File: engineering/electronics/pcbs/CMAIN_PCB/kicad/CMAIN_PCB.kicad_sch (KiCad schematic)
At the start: 73 parts, among them IC1 TSYS01, J1 RPI_5_WITH_SSQ-120-01-F-D, J10 1778719, J11 M9N-G4-3100, J12 1778719, J13 1778719, J14 XT30PW-F, J15 SM04B-GHS-TB_LF__SN_, J16 1778719, J17 SM03B-GHS-TB(LF)(SN), J18 SM04B-GHS-TB_LF__SN_, J19 1778719, J2 1778719, J20 SM04B-GHS-TB_LF__SN_, J21 1778719, J22 SM04B-GHS-TB_LF__SN_, J23 1814948, J24 1778719, J27 1814948, J29 1778735, J3 AXK6S00547YG, J30 1778735, J31 1814951, J32 1814948, J33 USB4216-03-A, J35 SM04B-GHS-TB_LF__SN_, J36 SM05B-GHS-TB_LF__SN_, J37 1778719, J38 1778719, J39 1814935, J4 AXK6S00547YG, J40 1814948, J41 SM06B-GHS-TB_LF__SN_, J43 1814948, J46 1814951, J49 1814935, J5 SM04B-GHS-TB_LF__SN_, J50 1814935, J53 1814935, J54 SM04B-GHS-TB_LF__SN_, J6 1778719, J7 SM04B-GHS-TB_LF__SN_, J8 1814935, J9 SM04B-GHS-TB_LF__SN_, U10 SMTSO25100CTJ, U11 SMTSO25100CTJ, U12 SMTSO25100CTJ, U3 SMTSOM380BTR, U5 C7429635, U6 SMTSOM380BTR, U7 SMTSOM380BTR, U8 SMTSOM380BTR, U9 SMTSO25100CTJ

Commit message: Import linked CMAIN PCB layout
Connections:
- net CAN2_H: now also R14.1, S2.1 (NC_1)
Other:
- sheet can_circuit renamed CAN_circuit
- sheet ethernet renamed Ethernet
- sheet power_control renamed Power_control
- sheet power_supply renamed Power_supply
- note added: "Temporary power-source flags for new power_supply architecture; replace with explicit hierarchical power pins once final regulator/distribution nets are locked."
- moved on the sheet: C1, IC1, J1, J10, J13, J15, J16, J18, J2, J20, J21, J22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

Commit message: electronics: update CMAIN and CBC PCB files
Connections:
- net CAN2_H: no longer R14.1, S2.1 (NC_1)
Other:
- moved on the sheet: J23, J27, J32, J40

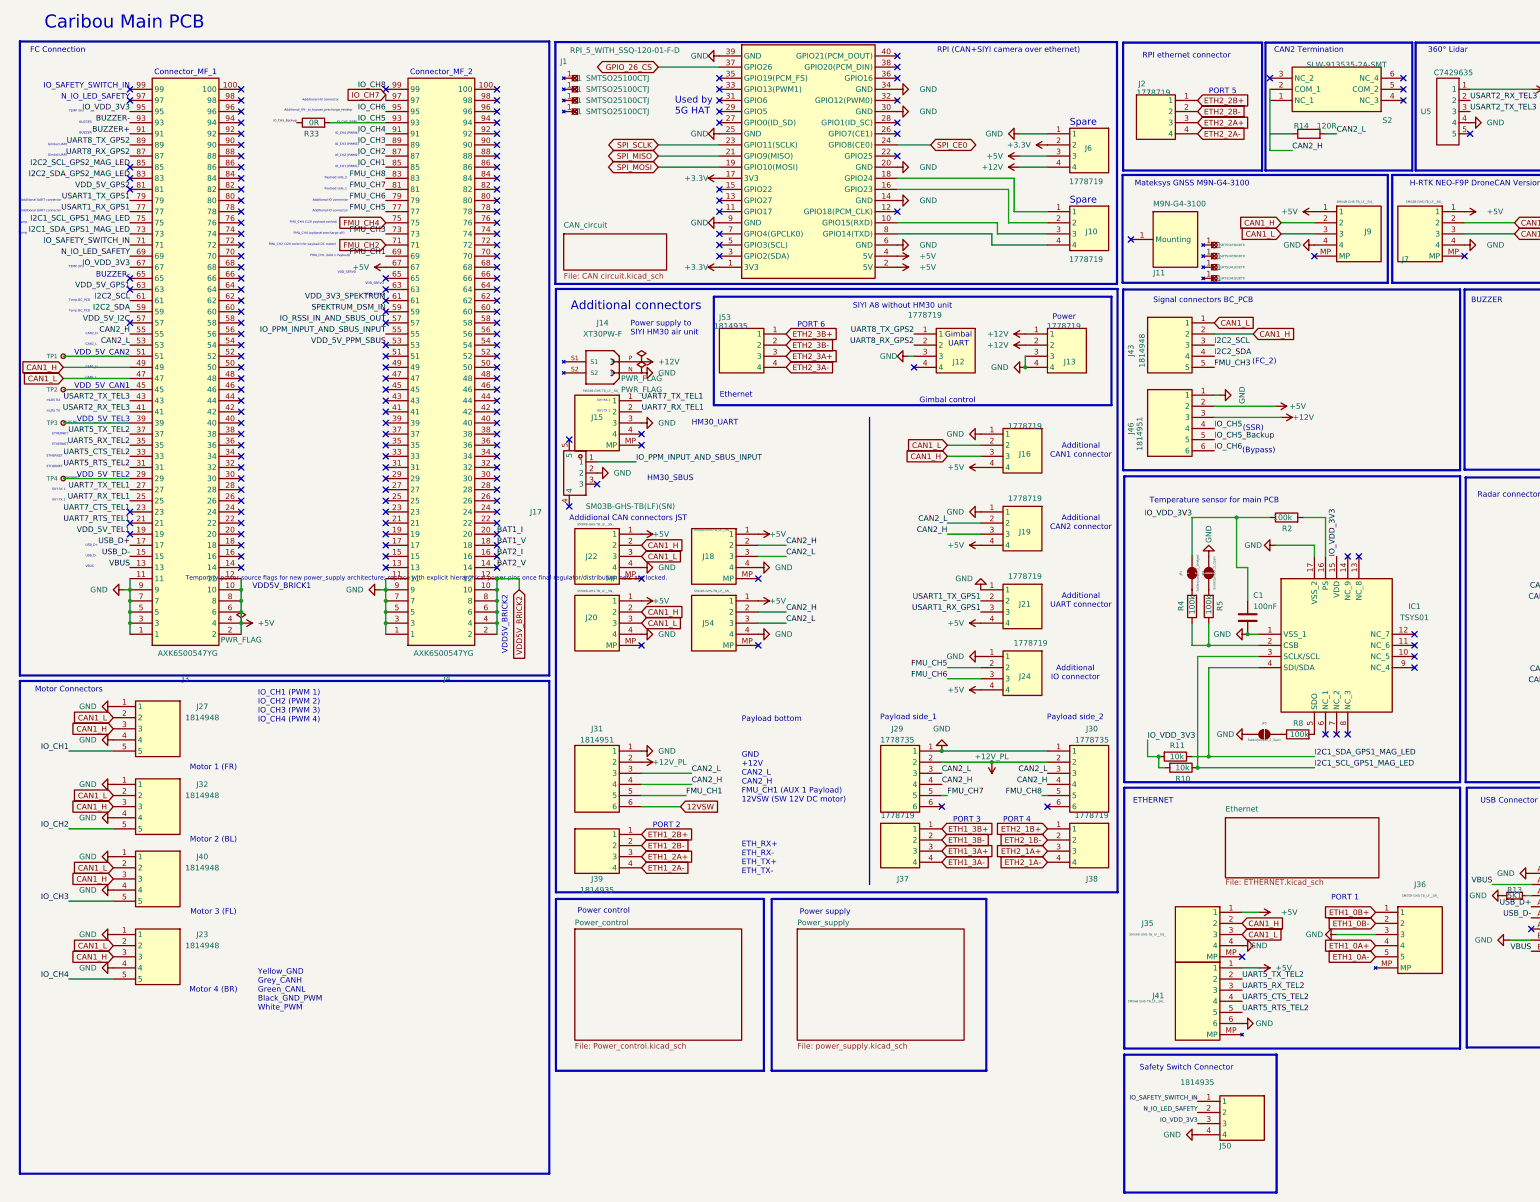
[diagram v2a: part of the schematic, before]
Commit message: electronics: integrate June PCB updates
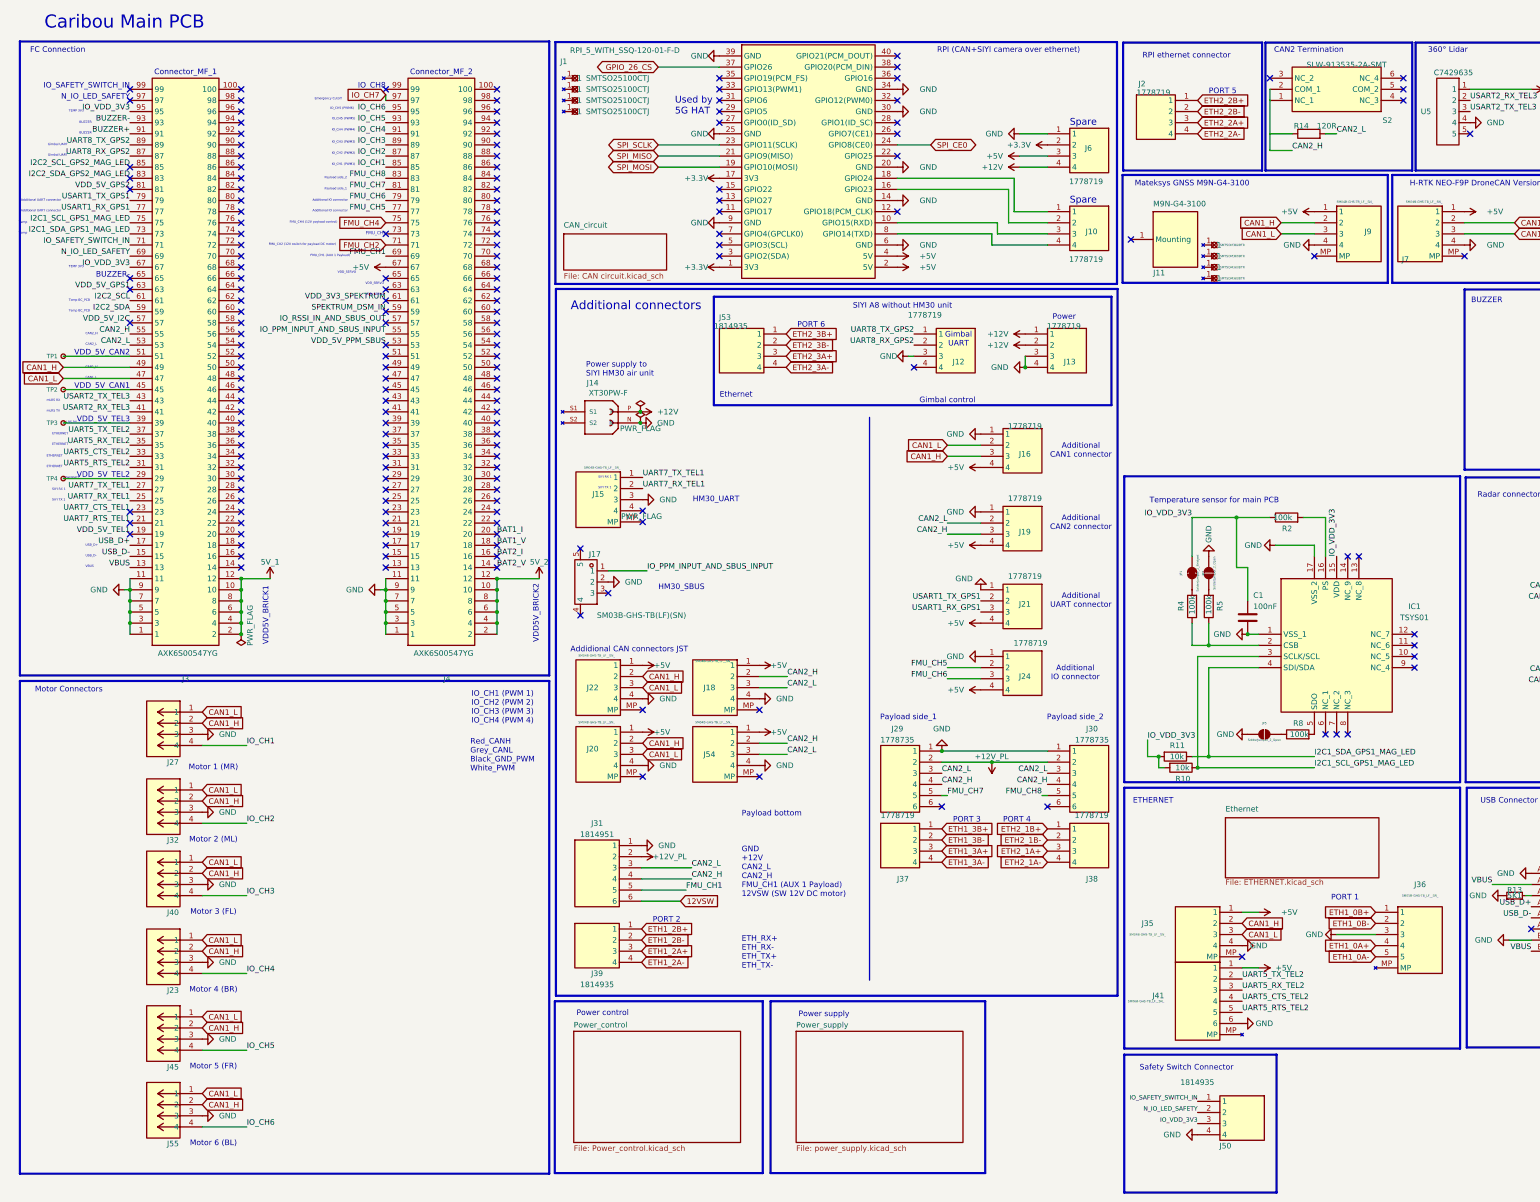
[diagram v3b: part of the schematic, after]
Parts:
- removed J43: 1814948, Samacsys:1814948, symbol Samacsys_kicad_sym:1814948
- removed J46: 1814951, Samacsys:1814951, symbol Samacsys_kicad_sym:1814951
- removed R33: 0R, Resistor_SMD:R_0805_2012Metric_Pad1.20x1.40mm_HandSolder, symbol Device:R
- added J45, J55: ${ALTIUM_VALUE}, CMAIN_PCB:AT13-4P, symbol CMAIN_PCB:AT13-4P
- J23, J27, J32, J40: value 1814948 -> ${ALTIUM_VALUE}; footprint Samacsys:1814948 -> CMAIN_PCB:AT13-4P; symbol Samacsys_kicad_sym:1814948 -> CMAIN_PCB:AT13-4P; Height 5.1 -> (none); MFR (none) -> Amphenol SINE Systems; MPN (none) -> AT13-4P; Manufacturer_Name Phoenix Contact -> (none); Manufacturer_Part_Number 1814948 -> (none); Mouser Part Number 651-1814948 -> (none); Mouser Price/Stock https://www.mouser.co.uk/ProductDetail/Phoenix-Contact/1814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 -> (none)
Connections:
- net +5V: no longer J3.10, J3.12, J3.2, J3.4, J3.6, J3.8
- net CAN1_H: now also J23.2, J27.2, J32.2, J40.2, J45.2, J55.2; no longer J23.3, J27.3, J32.3, J40.3
- net CAN1_L: now also J23.1, J27.1, J32.1, J40.1, J45.1, J55.1; no longer J23.2, J27.2, J32.2, J40.2
- net GND: now also J23.3, J27.3, J32.3, J40.3, J45.3, J55.3; no longer J23.1, J23.4, J27.1, J27.4, J32.1, J32.4, J40.1, J40.4
- net IO_CH1: now also J27.4; no longer J27.5
- net IO_CH2: now also J32.4; no longer J32.5
- net IO_CH3: now also J40.4; no longer J40.5
- net IO_CH4: now also J23.4; no longer J23.5
- net IO_CH5: now also J45.4
- net IO_CH6: now also J55.4
- net FMU_CH3: no longer names the net of J4.73
- net IO_CH8: no longer names the net of J4.99
- net VDD5V_BRICK2 renamed 5V_2
- new net 5V_1: J3.10, J3.12, J3.2, J3.4, J3.6, J3.8
- no-connect marks 182 -> 183
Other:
- note added: "Emergency Cutoff"
- note added: "FMU_CH3"
- note added: "IO_CH5 (PWM5)"
- note added: "IO_CH8"
- note added: "Motor 1 (MR)"
- note added: "Motor 2 (ML)"
- note added: "Motor 5 (FR)"
- note added: "Motor 6 (BL)"
- note added: "Red_CANH Grey_CANL Black_GND_PWM White_PWM"
- note removed: "(Bypass)"
- note removed: "(FC_2)"
- note removed: "(SSR)"
- note removed: "Additional HV connector"
- note removed: "FMU_CH4 (optional precharge off)"
- note removed: "IO_CH5 (SSR)"
- note removed: "Motor 1 (FR)"
- note removed: "Motor 2 (BL)"
- note removed: "Signal connectors BC_PCB"
- note removed: "Temporary power-source flags for new power_supply architecture; replace with explicit hierarchical power pins once final regulator/distribution nets are locked."
- note removed: "Yellow_GND Grey_CANH Green_CANL Black_GND_PWM White_PWM"
- moved on the sheet: J14, J15, J17, J18, J20, J22, J31, J39, J54

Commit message: electronics: clean up CMAIN local libraries
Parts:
- C1: footprint Capacitor_SMD:C_0805_2012Metric_Pad1.18x1.45mm_HandSolder -> CMAIN_PCB:C_0805_2012Metric_Pad1.18x1.45mm_HandSolder
- J14: footprint Snapeda:XT30PW-F_AMASS_XT30PW-F -> CMAIN_PCB:XT30PW-F_AMASS_XT30PW-F
- J15, J18, J20, J22, J35, J5, J54, J7: footprint Samacsys:SM04B-GHS-TB -> CMAIN_PCB:SM04B-GHS-TB
- J17: footprint EasyEDA_Lib:CONN-TH_SM03B-GHS-TB-LF-SN -> CMAIN_PCB:CONN-TH_SM03B-GHS-TB-LF-SN
- J23, J27, J32, J40: footprint CMAIN_PCB:AT13-4P -> CMAIN_PCB:1814948
- J29, J30: footprint Samacsys:1778735 -> CMAIN_PCB:1778735
- J3, J4: footprint Samacsys:AXK6S00547YG -> CMAIN_PCB:AXK6S00547YG
- J31: footprint Samacsys:1814951 -> CMAIN_PCB:1814951
- J33: footprint Samacsys:USB421603A -> CMAIN_PCB:USB421603A
- J36: footprint Samacsys:SM05B-GHS-TB -> CMAIN_PCB:SM05B-GHS-TB
- J39, J49, J50, J53, J8: footprint Samacsys:1814935 -> CMAIN_PCB:1814935
- J41: footprint Samacsys:SM06B-GHS-TB -> CMAIN_PCB:SM06B-GHS-TB
- J9: footprint Samacsys:SM04B-GHS-TB -> CMAIN_PCB:SM04B-GHS-TB_J9
- JP1: footprint Snapeda:SolderJumper-2_P1.3mm_Bridged2Bar_RoundedPad1.0x1.5mm -> CMAIN_PCB:SolderJumper-2_P1.3mm_Bridged2Bar_RoundedPad1.0x1.5mm
- JP2, JP5: footprint Snapeda:SolderJumper-2_P1.3mm_Open_RoundedPad1.0x1.5mm -> CMAIN_PCB:SolderJumper-2_P1.3mm_Open_RoundedPad1.0x1.5mm
- LS1: footprint Samacsys:CMT8530SSMTTR -> CMAIN_PCB:CMT8530SSMTTR
- R10, R11, R12, R13, R14, R2, R4, R5, R8: footprint Resistor_SMD:R_0805_2012Metric_Pad1.20x1.40mm_HandSolder -> CMAIN_PCB:R_0805_2012Metric_Pad1.20x1.40mm_HandSolder
- U5: footprint EasyEDA_Lib:CONN-TH_5P-P2.50_ZX-XH2.54-5PZZ -> CMAIN_PCB:CONN-TH_5P-P2.50_ZX-XH2.54-5PZZ
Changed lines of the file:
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@@
 			)
 		)
-		(property "Footprint" "Samacsys:SM04B-GHS-TB"
+		(property "Footprint" "CMAIN_PCB:SM04B-GHS-TB"
 			(at 275.59 314.96 0)
 			(hide yes)
@@
 			)
 		)
-		(property "Footprint" "Samacsys:1778735"
+		(property "Footprint" "CMAIN_PCB:1778735"
 			(at 264.16 278.13 0)
 			(hide yes)
@@
 			)
 		)
-		(property "Footprint" "Snapeda:SolderJumper-2_P1.3mm_Bridged2Bar_RoundedPad1.0x1.5mm"
+		(property "Footprint" "CMAIN_PCB:SolderJumper-2_P1.3mm_Bridged2Bar_RoundedPad1.0x1.5mm"
 			(at 280.67 142.24 0)
 			(hide yes)
@@
 			)
 		)
-		(property "Footprint" "Samacsys:AXK6S00547YG"
+		(property "Footprint" "CMAIN_PCB:AXK6S00547YG"
 			(at 118.11 62.23 0)
 			(hide yes)
@@
 			)
 		)
-		(property "Footprint" "Samacsys:SM04B-GHS-TB"
+		(property "Footprint" "CMAIN_PCB:SM04B-GHS-TB"
 			(at 326.39 154.94 0)
 			(hide yes)
@@
 			)
 		)
-		(property "Footprint" "Capacitor_SMD:C_0805_2012Metric_Pad1.18x1.45mm_HandSolder"
+		(property "Footprint" "CMAIN_PCB:C_0805_2012Metric_Pad1.18x1.45mm_HandSolder"
 			(at 294.64 156.21 0)
 			(hide yes)
@@
 			)
 		)
-		(property "Footprint" "Snapeda:SolderJumper-2_P1.3mm_Open_RoundedPad1.0x1.5mm"
+		(property "Footprint" "CMAIN_PCB:SolderJumper-2_P1.3mm_Open_RoundedPad1.0x1.5mm"
 			(at 297.18 179.07 0)
 			(hide yes)
@@
 			)
 		)
-		(property "Footprint" "Resistor_SMD:R_0805_2012Metric_Pad1.20x1.40mm_HandSolder"
+		(property "Footprint" "CMAIN_PCB:R_0805_2012Metric_Pad1.20x1.40mm_HandSolder"
 			(at 307.34 43.18 90)
 			(hide yes)
@@
 			)
 		)
-		(property "Footprint" "Samacsys:SM06B-GHS-TB"
+		(property "Footprint" "CMAIN_PCB:SM06B-GHS-TB"
 			(at 275.59 327.66 0)
 			(hide yes)
@@
 			)
 		)
-		(property "Footprint" "CMAIN_PCB:AT13-4P"
+		(property "Footprint" "CMAIN_PCB:1814948"
 			(at 39.116 213.868 0)
 			(hide yes)
@@
 			)
 		)
-		(property "Footprint" "Samacsys:SM04B-GHS-TB"
+		(property "Footprint" "CMAIN_PCB:SM04B-GHS-TB"
 			(at 138.684 214.376 0)
 			(hide yes)
@@
 			)
 		)
-		(property "Footprint" "Samacsys:SM04B-GHS-TB"
+		(property "Footprint" "CMAIN_PCB:SM04B-GHS-TB"
 			(at 165.354 258.572 0)
 			(hide yes)
@@
 			)
 		)
-		(property "Footprint" "Samacsys:SM04B-GHS-TB"
+		(property "Footprint" "CMAIN_PCB:SM04B-GHS-TB"
 			(at 363.22 154.94 0)
 			(hide yes)
@@
 			)
 		)
-		(property "Footprint" "Resistor_SMD:R_0805_2012Metric_Pad1.20x1.40mm_HandSolder"
+		(property "Footprint" "CMAIN_PCB:R_0805_2012Metric_Pad1.20x1.40mm_HandSolder"
 			(at 276.86 182.88 90)
 			(hide yes)
@@
 			)
 		)
-		(property "Footprint" "Snapeda:XT30PW-F_AMASS_XT30PW-F"
+		(property "Footprint" "CMAIN_PCB:XT30PW-F_AMASS_XT30PW-F"
 			(at 149.606 105.41 0)
 			(hide yes)
@@
 			)
 		)
-		(property "Footprint" "Samacsys:1814935"
+		(property "Footprint" "CMAIN_PCB:1814935"
 			(at 375.92 257.81 0)
 			(hide yes)
@@
 			)
 		)
-		(property "Footprint" "EasyEDA_Lib:CONN-TH_SM03B-GHS-TB-LF-SN"
+		(property "Footprint" "CMAIN_PCB:CONN-TH_SM03B-GHS-TB-LF-SN"
 			(at 143.51 144.272 0)
 			(hide yes)
@@
 			)
 		)
-		(property "Footprint" "Samacsys:SM05B-GHS-TB"
+		(property "Footprint" "CMAIN_PCB:SM05B-GHS-TB"
 			(at 339.09 314.96 0)
 			(hide yes)
@@
 			)
 		)
-		(property "Footprint" "Samacsys:SM04B-GHS-TB"
+		(property "Footprint" "CMAIN_PCB:SM04B-GHS-TB"
 			(at 138.684 272.542 0)
 			(hide yes)
@@
 			)
 		)
-		(property "Footprint" "Resistor_SMD:R_0805_2012Metric_Pad1.20x1.40mm_HandSolder"
+		(property "Footprint" "CMAIN_PCB:R_0805_2012Metric_Pad1.20x1.40mm_HandSolder"
 			(at 304.8 180.34 90)
 			(hide yes)
@@
 			)
 		)
-		(property "Footprint" "Resistor_SMD:R_0805_2012Metric_Pad1.20x1.40mm_HandSolder"
+		(property "Footprint" "CMAIN_PCB:R_0805_2012Metric_Pad1.20x1.40mm_HandSolder"
 			(at 397.51 210.82 0)
 			(hide yes)
@@
 			)
 		)
-		(property "Footprint" "Samacsys:SM04B-GHS-TB"
+		(property "Footprint" "CMAIN_PCB:SM04B-GHS-TB_J9"
 			(at 325.12 154.94 0)
 			(hide yes)
@@
 			)
 		)
-		(property "Footprint" "Samacsys:1814951"
+		(property "Footprint" "CMAIN_PCB:1814951"
 			(at 151.13 299.72 0)
 			(hide yes)
@@
 			)
 		)
-		(property "Footprint" "CMAIN_PCB:AT13-4P"
+		(property "Footprint" "CMAIN_PCB:1814948"
 			(at 39.116 179.578 0)
 			(hide yes)
@@
 			)
 		)
-		(property "Footprint" "EasyEDA_Lib:CONN-TH_5P-P2.50_ZX-XH2.54-5PZZ"
+		(property "Footprint" "CMAIN_PCB:CONN-TH_5P-P2.50_ZX-XH2.54-5PZZ"
 			(at 339.09 36.83 0)
 			(hide yes)
@@
 			)
 		)
-		(property "Footprint" "Samacsys:1814935"
+		(property "Footprint" "CMAIN_PCB:1814935"
 			(at 285.75 356.87 0)
 			(hide yes)
@@
 			)
 		)
-		(property "Footprint" "Samacsys:1814935"
+		(property "Footprint" "CMAIN_PCB:1814935"
 			(at 151.13 318.77 0)
 			(hide yes)
@@
 			)
 		)
-		(property "Footprint" "Samacsys:USB421603A"
+		(property "Footprint" "CMAIN_PCB:USB421603A"
 			(at 389.89 306.07 0)
 			(hide yes)
@@
 			)
 		)
-		(property "Footprint" "Samacsys:AXK6S00547YG"
+		(property "Footprint" "CMAIN_PCB:AXK6S00547YG"
 			(at 59.69 62.23 0)
 			(hide yes)
@@
 			)
 		)
-		(property "Footprint" "Samacsys:1778735"
+		(property "Footprint" "CMAIN_PCB:1778735"
 			(at 207.01 278.13 0)
 			(hide yes)
@@
 			)
 		)
-		(property "Footprint" "Samacsys:SM04B-GHS-TB"
+		(property "Footprint" "CMAIN_PCB:SM04B-GHS-TB"
 			(at 165.354 273.812 0)
 			(hide yes)
@@
 			)
 		)
-		(property "Footprint" "Samacsys:SM04B-GHS-TB"
+		(property "Footprint" "CMAIN_PCB:SM04B-GHS-TB"
 			(at 138.684 258.572 0)
 			(hide yes)
@@
 			)
 		)
-		(property "Footprint" "Snapeda:SolderJumper-2_P1.3mm_Open_RoundedPad1.0x1.5mm"
+		(property "Footprint" "CMAIN_PCB:SolderJumper-2_P1.3mm_Open_RoundedPad1.0x1.5mm"
 			(at 284.48 142.24 0)
 			(hide yes)
@@
 			)
 		)
-		(property "Footprint" "CMAIN_PCB:AT13-4P"
+		(property "Footprint" "CMAIN_PCB:1814948"
 			(at 39.116 161.798 0)
 			(hide yes)
@@
 			)
 		)
-		(property "Footprint" "Samacsys:1814935"
+		(property "Footprint" "CMAIN_PCB:1814935"
 			(at 184.15 182.88 0)
 			(hide yes)
@@
 			)
 		)
-		(property "Footprint" "Resistor_SMD:R_0805_2012Metric_Pad1.20x1.40mm_HandSolder"
+		(property "Footprint" "CMAIN_PCB:R_0805_2012Metric_Pad1.20x1.40mm_HandSolder"
 			(at 354.33 215.9 0)
 			(hide yes)
@@
 			)
 		)
-		(property "Footprint" "Resistor_SMD:R_0805_2012Metric_Pad1.20x1.40mm_HandSolder"
+		(property "Footprint" "CMAIN_PCB:R_0805_2012Metric_Pad1.20x1.40mm_HandSolder"
 			(at 278.13 185.42 90)
 			(hide yes)
@@
 			)
 		)
-		(property "Footprint" "Samacsys:CMT8530SSMTTR"
+		(property "Footprint" "CMAIN_PCB:CMT8530SSMTTR"
 			(at 384.81 190.5 0)
 			(hide yes)
@@
 			)
 		)
-		(property "Footprint" "Resistor_SMD:R_0805_2012Metric_Pad1.20x1.40mm_HandSolder"
+		(property "Footprint" "CMAIN_PCB:R_0805_2012Metric_Pad1.20x1.40mm_HandSolder"
 			(at 281.94 149.86 90)
 			(hide yes)
@@
 			)
 		)
-		(property "Footprint" "Resistor_SMD:R_0805_2012Metric_Pad1.20x1.40mm_HandSolder"
+		(property "Footprint" "CMAIN_PCB:R_0805_2012Metric_Pad1.20x1.40mm_HandSolder"
 			(at 302.26 130.81 90)
 			(hide yes)
@@
 			)
 		)
-		(property "Footprint" "Samacsys:1814935"
+		(property "Footprint" "CMAIN_PCB:1814935"
 			(at 375.92 238.76 0)
 			(hide yes)
@@
 			)
 		)
-		(property "Footprint" "Resistor_SMD:R_0805_2012Metric_Pad1.20x1.40mm_HandSolder"
+		(property "Footprint" "CMAIN_PCB:R_0805_2012Metric_Pad1.20x1.40mm_HandSolder"
 			(at 285.75 149.86 90)
 			(hide yes)
@@
 			)
 		)
-		(property "Footprint" "CMAIN_PCB:AT13-4P"
+		(property "Footprint" "CMAIN_PCB:1814948"
 			(at 39.116 196.088 0)
 			(hide yes)
